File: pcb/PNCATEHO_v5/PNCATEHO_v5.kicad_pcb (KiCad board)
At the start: 2 copper layers, 94.6 x 55 mm, 27 parts, among them J1 TestPoint_2Pole, SW1 SW_PUSH, SW10 SW_PUSH, SW2 SW_PUSH, SW3 SW_PUSH, SW4 SW_PUSH, SW5 SW_PUSH, SW6 SW_PUSH, SW7 SW_PUSH, SW8 SW_PUSH, SW9 SW_PUSH, U1 ProMicro_r

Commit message: Basic layout
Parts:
- moved PSW1 55.5 mm to (114.1, 25.9), turned to 0 degrees
- moved RSW1 31.1 mm to (114.1, 62.6), turned to 0 degrees
- moved H3 3.04 mm to (103.5, 64.5)
- moved H1 2.69 mm to (46.5, 45.5)
- moved H2 1.12 mm to (84.5, 45.5)
- moved J1 1.00 mm to (114.1, 42.8)
- moved U1 1.00 mm to (114.1, 42.8)
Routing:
- net GND: track 63.3 -> 1.43 mm, vias 2 -> 0
- net Net-(PSW1-B): track 67.9 -> 12.0 mm
- net VBAT: track 64.7 -> 14.1 mm, vias 1 -> 2
- net Net-(LED3-DOUT): track 0.00 -> 35.5 mm, vias 0 -> 2
- net R2C1: track 77.8 -> 111.7 mm, vias 1 -> 3
- net R2C2: track 69.4 -> 91.2 mm, vias 1 -> 3
- net reset: track 59.7 -> 38.6 mm, vias 0 -> 1
- net R1C3: track 40.6 -> 60.1 mm, vias 1 -> 2
- net R1C1: track 81.2 -> 100.2 mm, vias 1 -> 3
- net R1C4: track 21.6 -> 40.6 mm, vias 1 -> 2
- net R1C2: track 59.1 -> 77.7 mm, vias 1 -> 2
- net R2C3: track 48.8 -> 66.4 mm, vias 1 -> 3
- net R2C4: track 28.3 -> 45.4 mm, vias 1 -> 3
- net R3C5: track 39.8 -> 55.0 mm, vias 1 -> 3
- net LED: track 23.2 -> 36.1 mm, vias 1 -> 2
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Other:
- board size 94.6 x 55 mm -> 97 x 59 mm

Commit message: v5 ready for production?
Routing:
- net LED: track 36.1 -> 50.0 mm
- net Net-(LED1-DOUT): track 21.4 -> 35.1 mm, vias 1 -> 2
- net unconnected-(LED10-DOUT-Pad2)_1: track 7.00 -> 0.00 mm, vias 1 -> 0
- net VCC: track 248.9 -> 254.2 mm
- net GND: track 1.43 -> 6.53 mm
- net R3C5: track 55.0 -> 50.8 mm, vias 3 -> 2
- net Net-(PSW1-B): track 12.0 -> 8.98 mm
- net R2C4: track 45.4 -> 48.1 mm
- net VBAT: track 14.1 -> 11.9 mm, vias 2 -> 1
- net R2C3: track 66.4 -> 68.2 mm
- net R1C4: track 40.6 -> 42.4 mm
- net R2C1: track 111.7 -> 113.3 mm
- net R1C2: track 77.7 -> 79.0 mm
- net R1C3: track 60.1 -> 61.2 mm
- net R1C1: track 100.2 -> 100.3 mm, vias 3 -> 2

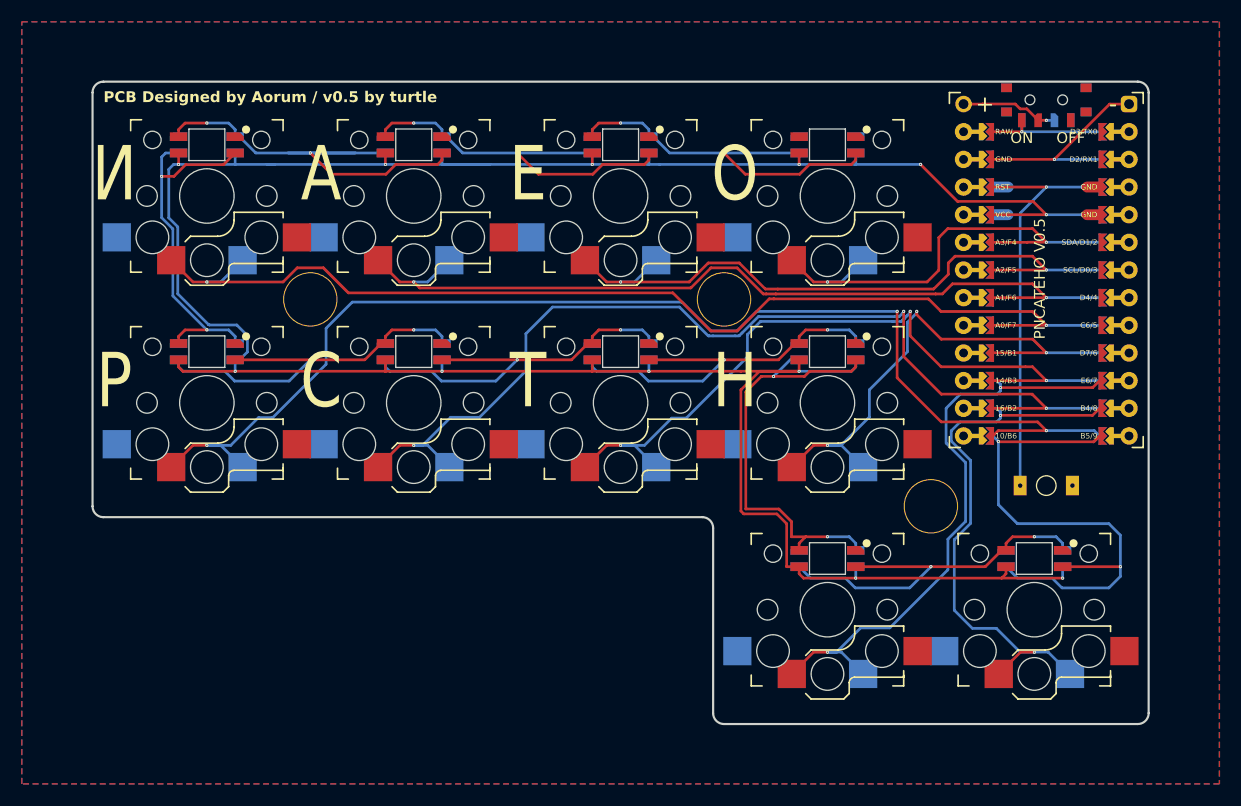
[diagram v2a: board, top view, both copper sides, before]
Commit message: Changed vias to 0.3/0.5
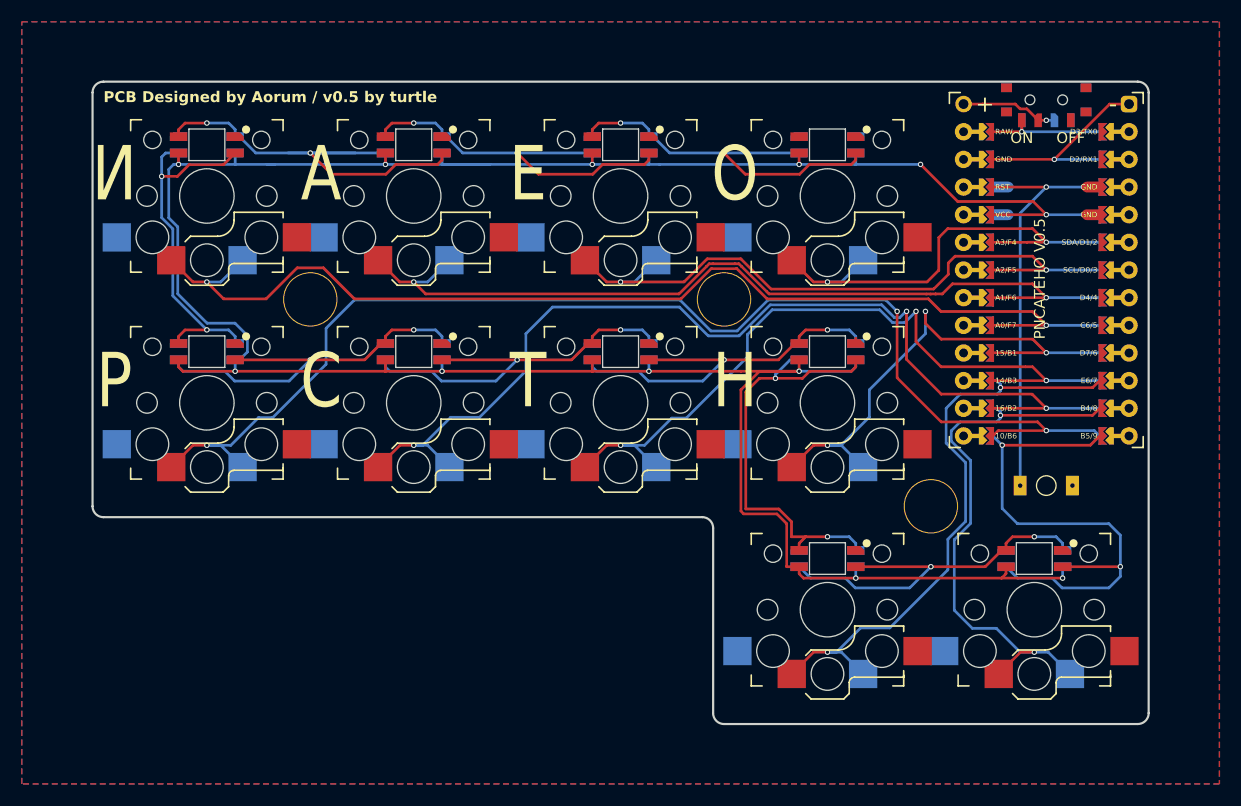
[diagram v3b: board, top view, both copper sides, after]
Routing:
- net R1C1: track 100.3 -> 101.4 mm
- net R2C2: track 91.6 -> 92.7 mm
- net R2C1: track 113.3 -> 114.4 mm
- net LED: track 50.0 -> 49.0 mm
- net R1C2: track 79.0 -> 79.8 mm

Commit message: Small beauty fix
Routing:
- net Net-(LED2-DOUT): track 39.9 -> 39.0 mm
- net VCC: track 254.2 -> 253.2 mm

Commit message: v0.5.1 100x100 version pcb
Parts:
- U1: footprint PNCATEHO:ProMicro_duplex -> PNCATEHO:ProMicro_duplex_mirrored
- moved RSW1 1.10 mm to (114.1, 61.5)
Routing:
- net R2C2: track 92.7 -> 97.0 mm, vias 3 -> 4
- net R2C4: track 48.1 -> 51.6 mm
- net R3C5: track 50.8 -> 48.1 mm, vias 2 -> 4
- net R2C1: track 114.4 -> 116.8 mm, vias 3 -> 4
- net R3C4: track 55.1 -> 53.2 mm, vias 2 -> 3
- net Net-(LED2-DOUT): track 39.0 -> 40.3 mm
- net LED: track 49.0 -> 47.7 mm
- net reset: track 38.2 -> 37.1 mm
- net R1C3: track 61.5 -> 62.6 mm
- net VCC: track 253.2 -> 252.2 mm, vias 12 -> 11
- net R1C4: track 42.4 -> 43.2 mm
- net R2C3: track 68.7 -> 69.2 mm, vias 3 -> 4
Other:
- board text added: "A"
- board text added: "C"
- board text added: "E"
- board text added: "H"
- board text added: "N"
- board text added: "O"
- board text added: "P"
- board text added: "PCB Designed by Aorum / v0.5.1 by turtle"
- board text added: "PNCATEHO V0.5.1"
- board text added: "T"
- board text removed: "PCB Designed by Aorum / v0.5 by turtle"
- board text removed: "PNCATEHO V0.5"
- board text removed: "А"
- board text removed: "Е"
- board text removed: "И"
- board text removed: "Н"
- board text removed: "О"
- board text removed: "Р"
- board text removed: "С"
- board text removed: "Т"
